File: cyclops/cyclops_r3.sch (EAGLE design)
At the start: 133 parts, among them Q1 BC817, Q2 IRF510, U1 MCP4921, U10 TLV2374, U11 THS4281, U12 MAX4564, U13 ZXTD, U14 ZXTD, U2 ADG3301, U3 MCP4022-50k, U4 LT1931, U5 LT1764A, U6 337L, U7 TLV3701, U8 ADR03, U9 OP1177, X1 SLP3, X2 SLP3, X3 SLP3

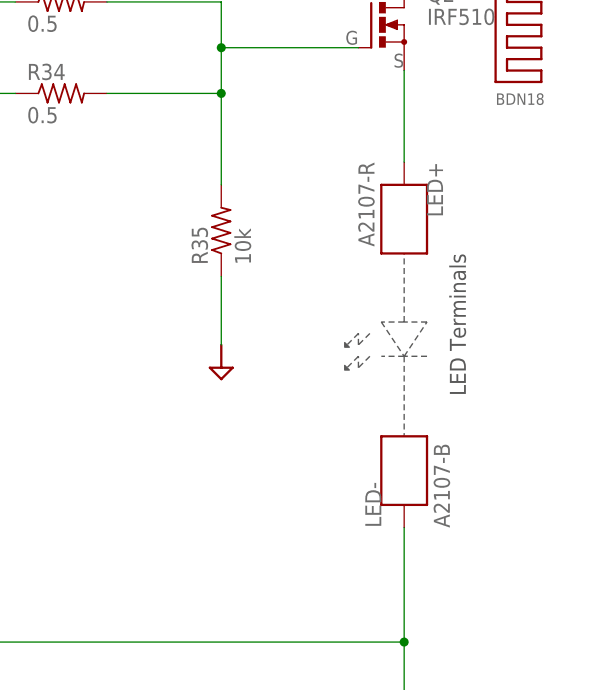
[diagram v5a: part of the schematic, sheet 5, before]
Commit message: A few changes made to comply with CircuitHub stuff
- Almost ready to do a circuit hub run.
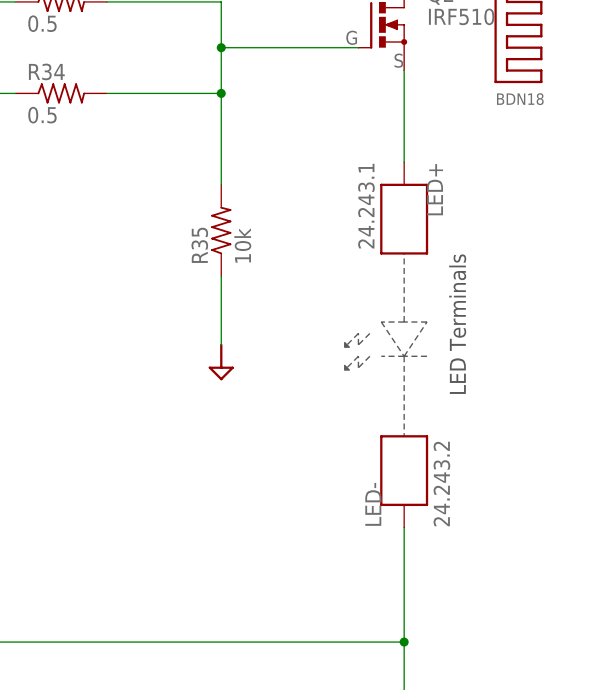
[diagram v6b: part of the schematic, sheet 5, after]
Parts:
- COMP: value ORG -> RED
- LED+: value A2107-R -> 24.243.1
- LED-: value A2107-B -> 24.243.2
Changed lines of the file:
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@@
 <part name="U$43" library="cyclops" deviceset="GND2" device=""/>
 <part name="R23" library="cyclops" deviceset="R" device="_0603" value="2.2k"/>
-<part name="LED-" library="cyclops" deviceset="BANANA_TO_BOARD" device="_A2107" value="A2107-B"/>
-<part name="LED+" library="cyclops" deviceset="BANANA_TO_BOARD" device="_A2107" value="A2107-R"/>
+<part name="LED-" library="cyclops" deviceset="BANANA_TO_BOARD" device="_A2107" value="24.243.2"/>
+<part name="LED+" library="cyclops" deviceset="BANANA_TO_BOARD" device="_A2107" value="24.243.1"/>
 <part name="R17" library="cyclops" deviceset="R" device="_0603" value="1k"/>
 <part name="R18" library="cyclops" deviceset="R" device="_0603" value="1k"/>
@@
 <part name="C8" library="cyclops" deviceset="C" device="_0603" value=".1uF"/>
 <part name="R16" library="cyclops" deviceset="R" device="_0603" value="470"/>
-<part name="COMP" library="cyclops" deviceset="LED" device="_0603" value="ORG"/>
+<part name="COMP" library="cyclops" deviceset="LED" device="_0603" value="RED"/>
 <part name="U$49" library="cyclops" deviceset="GND2" device=""/>
 <part name="L3" library="cyclops" deviceset="L" device="_0603" value="MPZ1608"/>

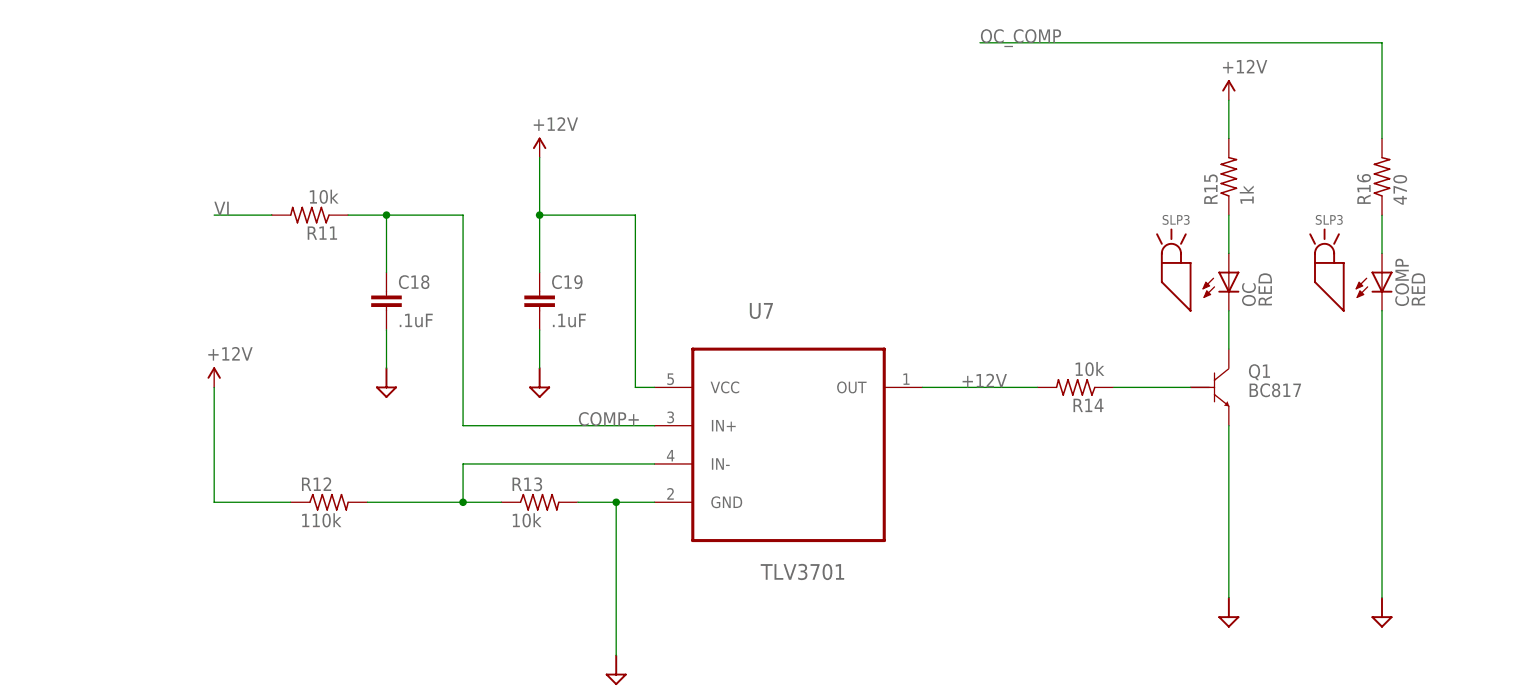
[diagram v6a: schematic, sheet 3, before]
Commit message: Reworked overcurrent circuit.
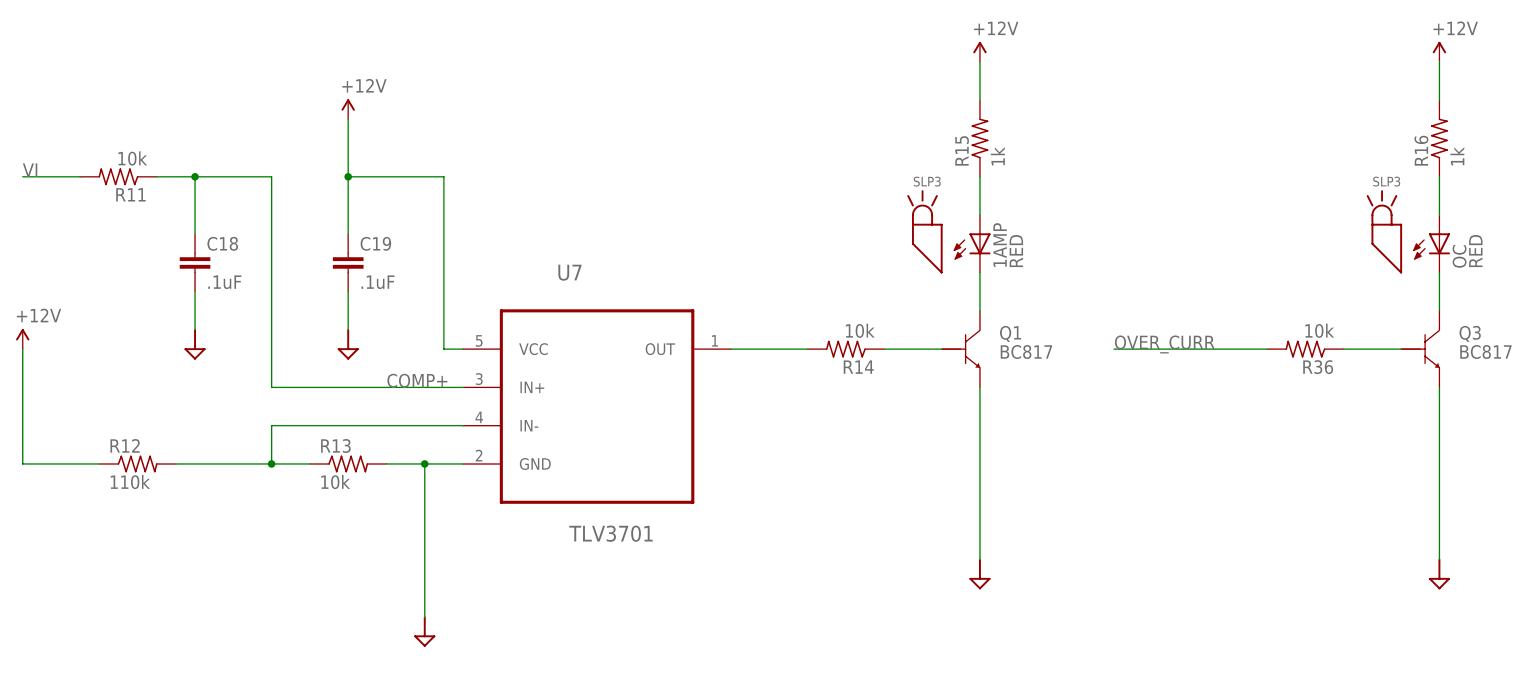
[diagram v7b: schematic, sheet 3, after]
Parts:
- removed C8: .1uF, cyclops:C_0603
- removed COMP: RED, cyclops:LED_0603
- removed SJ1: (no value), jonnew:SJ2_0603
- added 1AMP: RED, cyclops:LED_0603
- added C14, C36: 10nF, cyclops:C_0603
- added Q3: BC817, cyclops:BC817-16SMD
- added R21, R36: 10k, cyclops:R_0603
- R16: value 470 -> 1k
- U3: value MCP4022-50k -> MAX4564; device cyclops:MCP4022 -> cyclops:MAX4564
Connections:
- removed net OC_COMP: LEONARDO.D2, R16.2
- removed net POT: LEONARDO.D12, U3.U/~D
- removed net VCTL_FIXED: R23.2, SJ1.1
- new net N$39: Q3.B, R36.1
- new net OVER_CURR: LEONARDO.D2, R21.1, R36.2, U3.IN
- new net VCTL_PROT: R23.2, U3.NC
- net +12V: now also C36.1, R16.2, U3.V+
- net +5V: no longer C8.1, U3.VDD
- net -1.25V: now also C14.1, U3.V-
- net CS: no longer U3.~CS
- net GND: now also C14.2, C36.2, Q3.E, R21.2, U3.GND, U3.NO, U3.~EN; no longer C8.2, COMP.C, U3.VSS
- net N$16: now also OC.A; no longer COMP.A
- net N$2: now also 1AMP.A; no longer OC.A
- net N$38: now also OC.C, Q3.C; no longer SJ1.2, U3.A
- net N$9: now also 1AMP.C; no longer OC.C
- net VCTL: now also U3.COM; no longer SJ1.COM
- net VCTL_PROTECT: no longer U3.W
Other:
- moved on the sheet: C18, C19, GAIN, OC, Q1, R11, R12, R13, R14, R15, R16, R22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

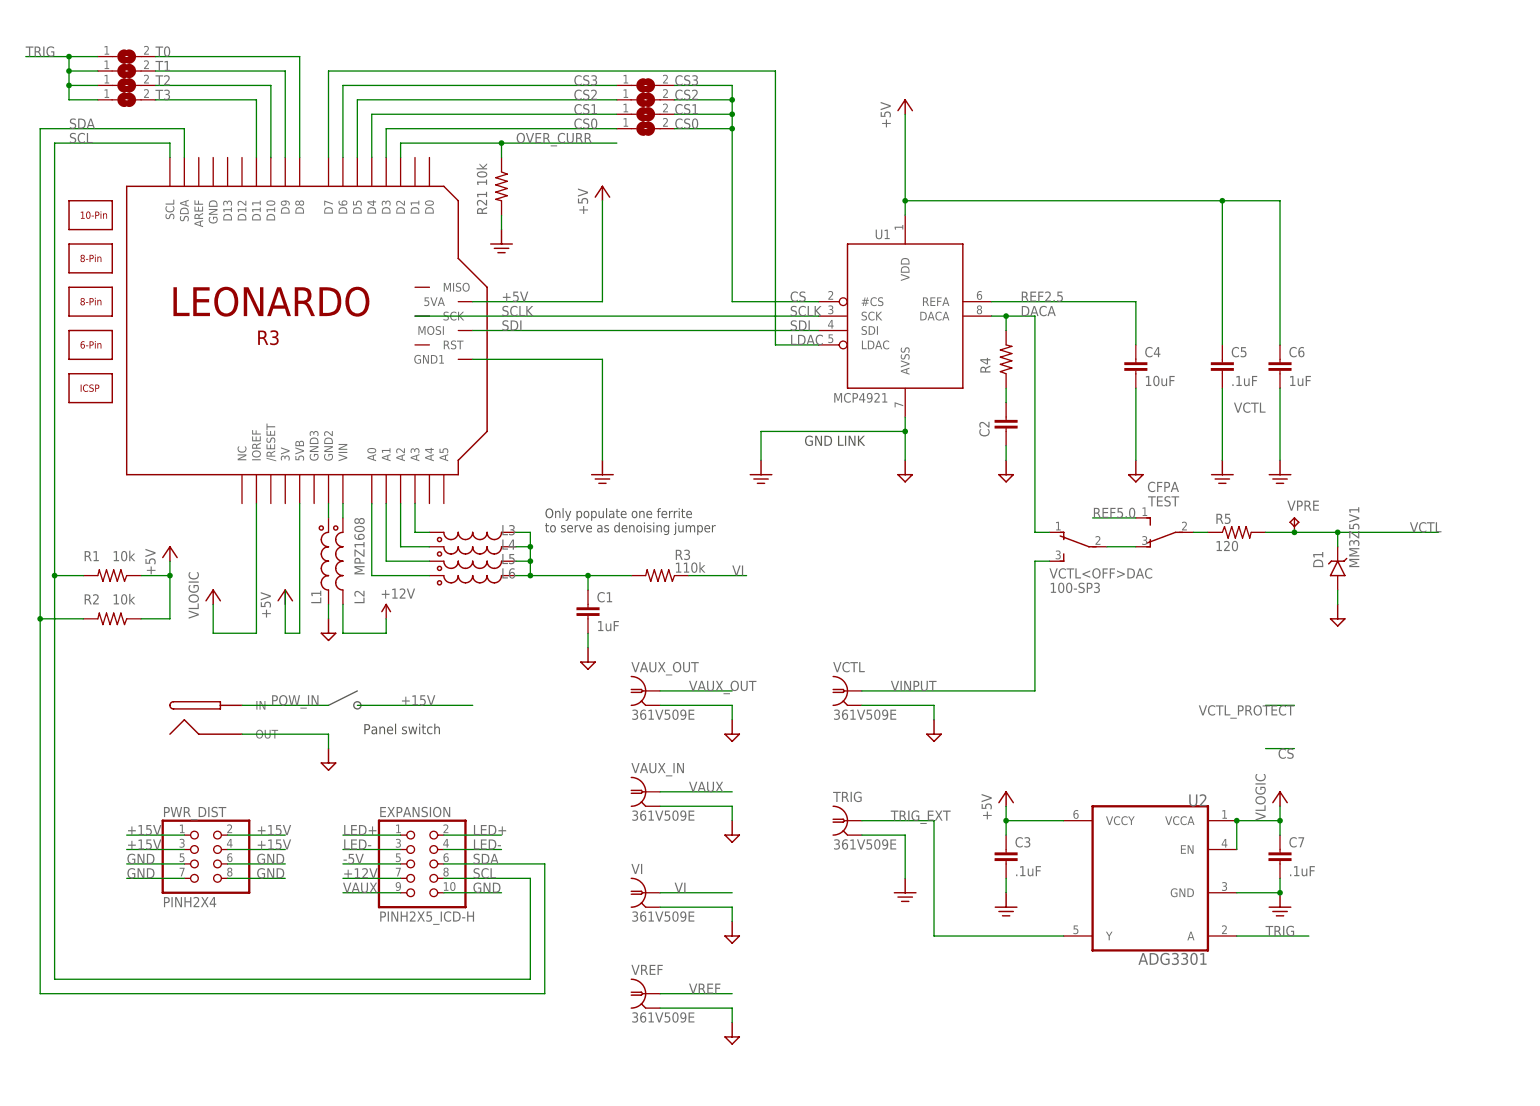
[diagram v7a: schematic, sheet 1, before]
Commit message: Further improvements to overcurrent circuitry.
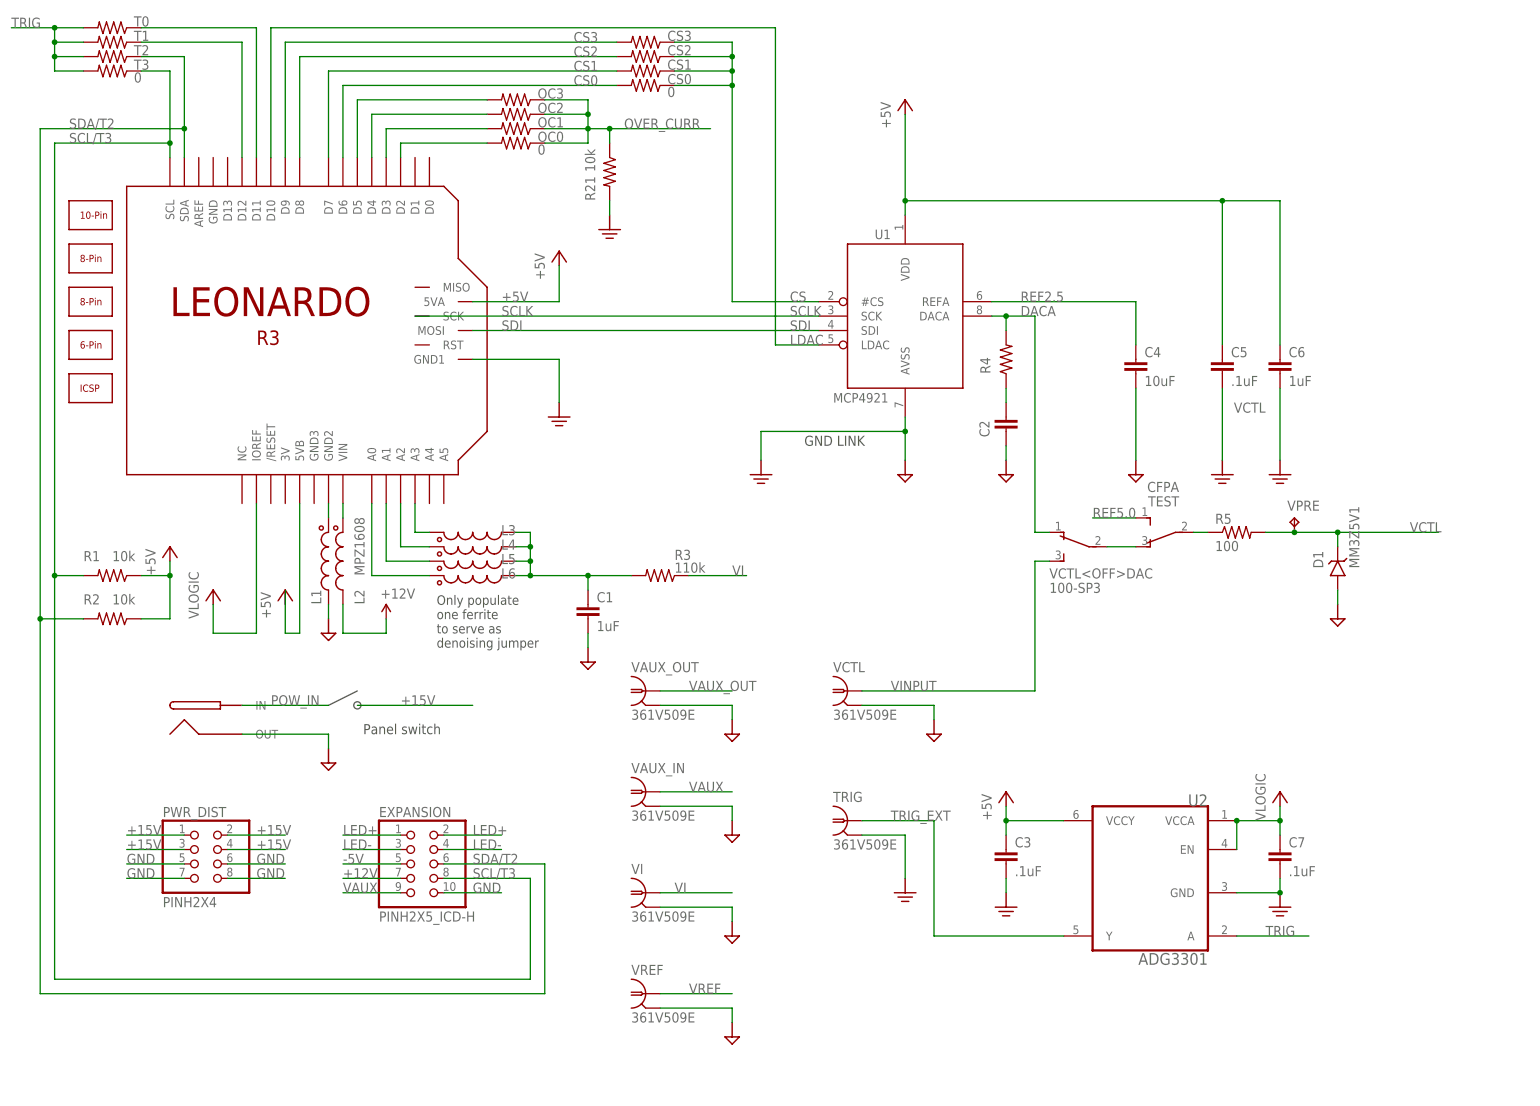
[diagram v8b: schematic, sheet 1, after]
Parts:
- added OC0, OC1, OC2, OC3: 0, cyclops:R_0603
- CS0, CS1, CS2, CS3, T0, T1, T2, T3: value (none) -> 0; device cyclops:SJ -> cyclops:R_0603
- R5: value 120 -> 100
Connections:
- removed net SCL: EXPANSION.8, LEONARDO.SCL, R1.2
- removed net SDA: EXPANSION.6, LEONARDO.SDA, R2.2
- removed net T2: LEONARDO.D10, T2.2
- removed net T3: LEONARDO.D11, T3.2
- new net N$40: LEONARDO.D2, OC0.2
- new net OC0: LEONARDO.D3, OC1.2
- new net OC1: LEONARDO.D4, OC2.2
- new net OC2: LEONARDO.D5, OC3.2
- new net SCL/T3: EXPANSION.8, LEONARDO.SCL, R1.2, T3.1
- new net SDA/T2: EXPANSION.6, LEONARDO.SDA, R2.2, T2.1
- net CS: now also CS0.1, CS1.1, CS2.1, CS3.1; no longer CS0.2, CS1.2, CS2.2, CS3.2
- net CS0: now also CS0.2, LEONARDO.D6; no longer CS0.1, LEONARDO.D3
- net CS1: now also CS1.2, LEONARDO.D7; no longer CS1.1, LEONARDO.D4
- net CS2: now also CS2.2, LEONARDO.D8; no longer CS2.1, LEONARDO.D5
- net CS3: now also CS3.2, LEONARDO.D9; no longer CS3.1, LEONARDO.D6
- net LDAC: now also LEONARDO.D10; no longer LEONARDO.D7
- net OVER_CURR: now also OC0.1, OC1.1, OC2.1, OC3.1; no longer LEONARDO.D2
- net T0: now also LEONARDO.D11, T0.1; no longer LEONARDO.D8, T0.2
- net T1: now also LEONARDO.D12, T1.1; no longer LEONARDO.D9, T1.2
- net TRIG: now also T0.2, T1.2, T2.2, T3.2; no longer T0.1, T1.1, T2.1, T3.1
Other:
- moved on the sheet: R21
